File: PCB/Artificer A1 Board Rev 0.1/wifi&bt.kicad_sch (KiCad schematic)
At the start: 14 parts

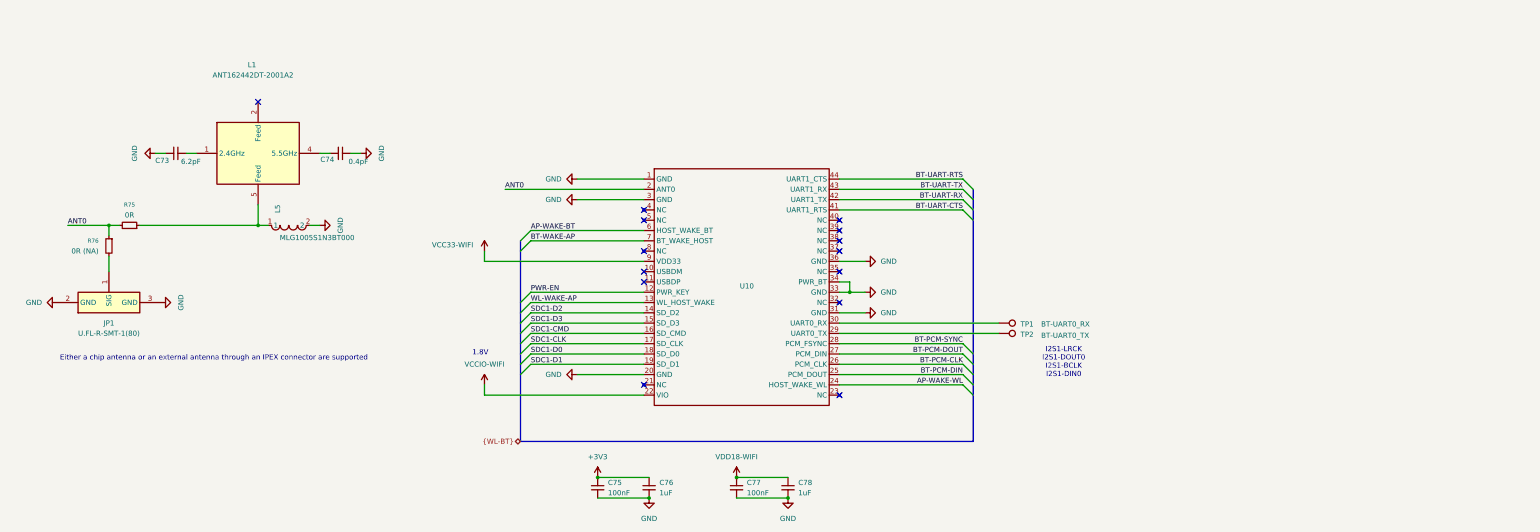
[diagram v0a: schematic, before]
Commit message: cleaned up, kicad 10 & usb c pd
migrated to Kicad 10,
added USB PD for power input
added capacitors inductors and resistor footprints
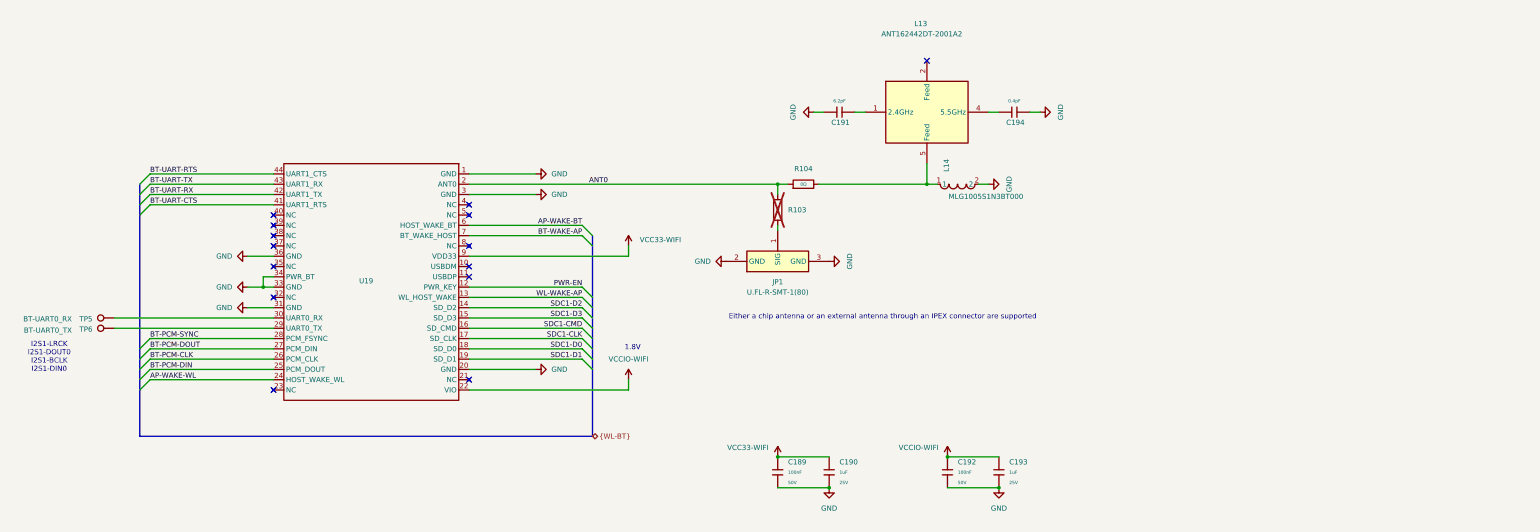
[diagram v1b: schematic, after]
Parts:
- removed C73: 6.2pF, symbol Device:C_Small
- removed C74: 0.4pF, symbol Device:C_Small
- removed C75, C77: 100nF, symbol Device:C_Small
- removed C76, C78: 1uF, symbol Device:C_Small
- removed R75: 0R, symbol Device:R_Small
- removed R76: 0R (NA), symbol Device:R_Small
- added C189, C192: 100nF, PCM_JLCPCB:C_0402, symbol PCM_JLCPCB-Capacitors:0402,100nF,(2)
- added C190, C193: 1uF, PCM_JLCPCB:C_0402, symbol PCM_JLCPCB-Capacitors:0402,1uF
- added C191: 6.2pF, PCM_JLCPCB:C_0402, symbol PCM_JLCPCB-Capacitors:0402,1pF
- added C194: 0.4pF, PCM_JLCPCB:C_0402, symbol PCM_JLCPCB-Capacitors:0402,1pF
- added R103, R104: 0Ω, PCM_JLCPCB:R_0402, symbol PCM_JLCPCB-Resistors:0402,0Ω
- U19: renamed from U10; value ~ -> (none)
- renumbered L1 to L13, L5 to L14, TP1 to TP5, TP2 to TP6
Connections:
- net ANT0: now also R103.2, R104.1
- net GND: now also C189.2, C190.2, C191.2, C192.2, C193.2, C194.1
- net VCC33-WIFI: now also C189.1, C190.1
- net VCCIO-WIFI: now also C192.1, C193.1
- net at JP1.1 (SIG): now also R103.1
- net at L13.1 (2.4GHz): now also C191.1
- net at L13.4 (5.5GHz): now also C194.2
- net at L13.5 (Feed), L14.1: now also R104.2
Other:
- moved on the sheet: JP1, L13, L14, TP5, TP6, U19

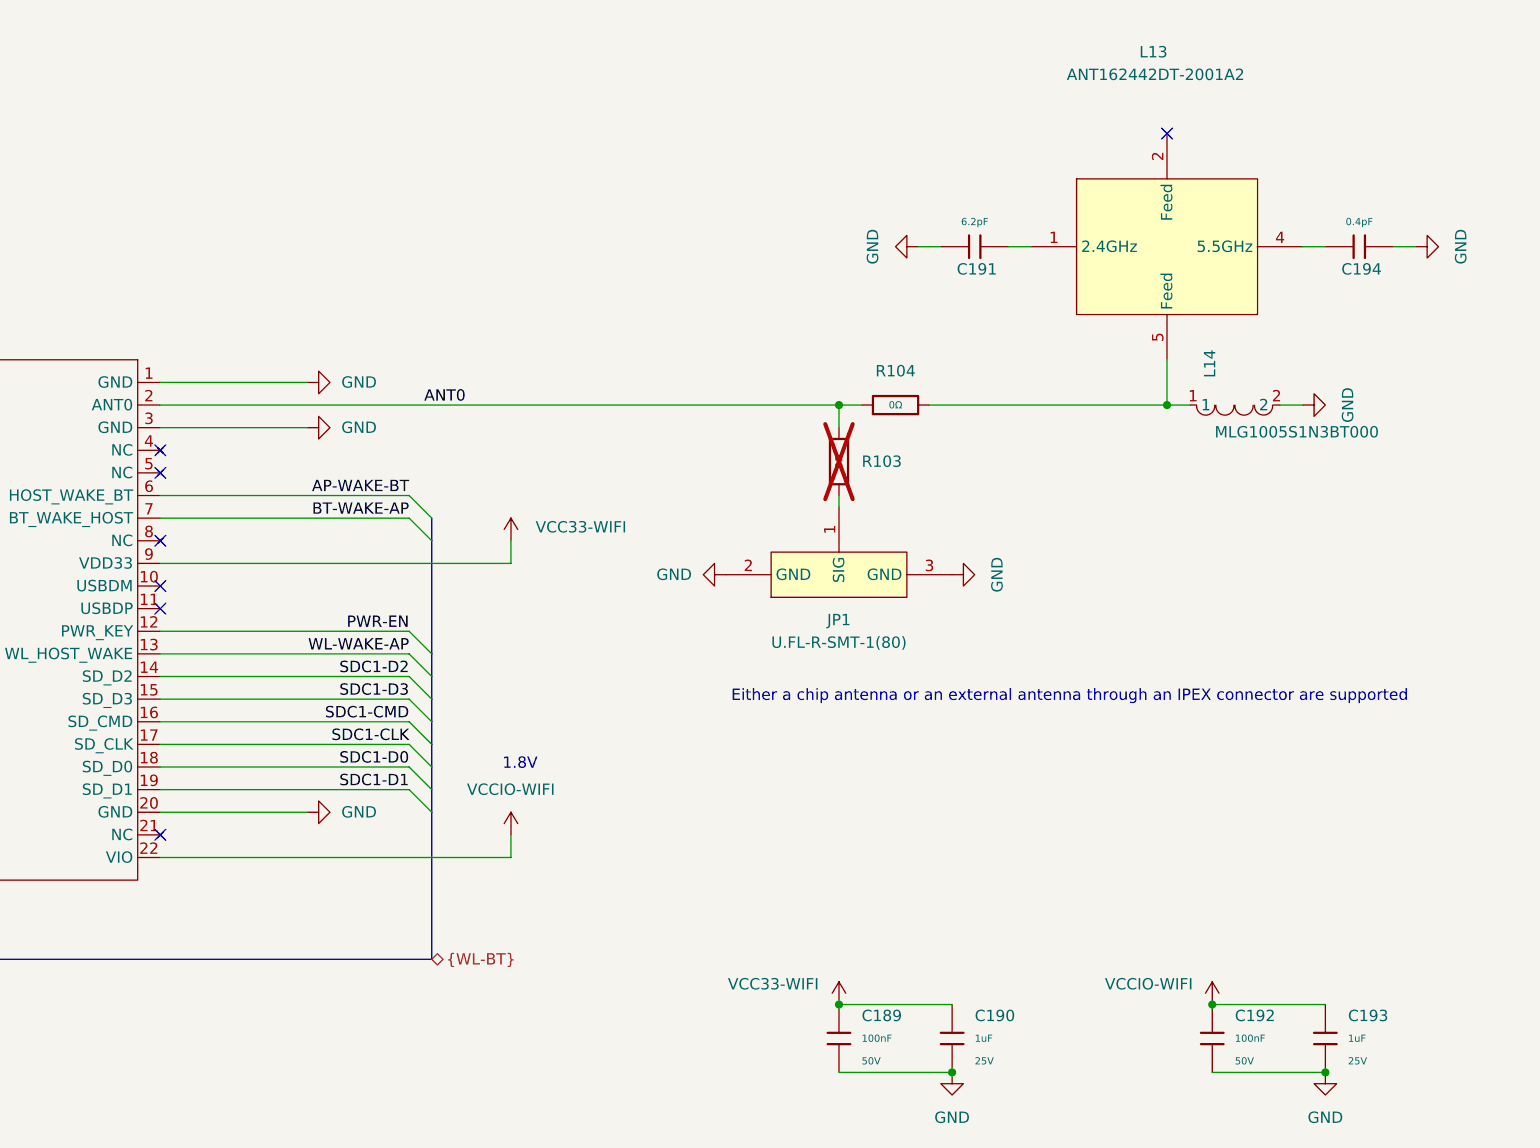
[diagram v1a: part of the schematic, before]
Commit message: placed all components
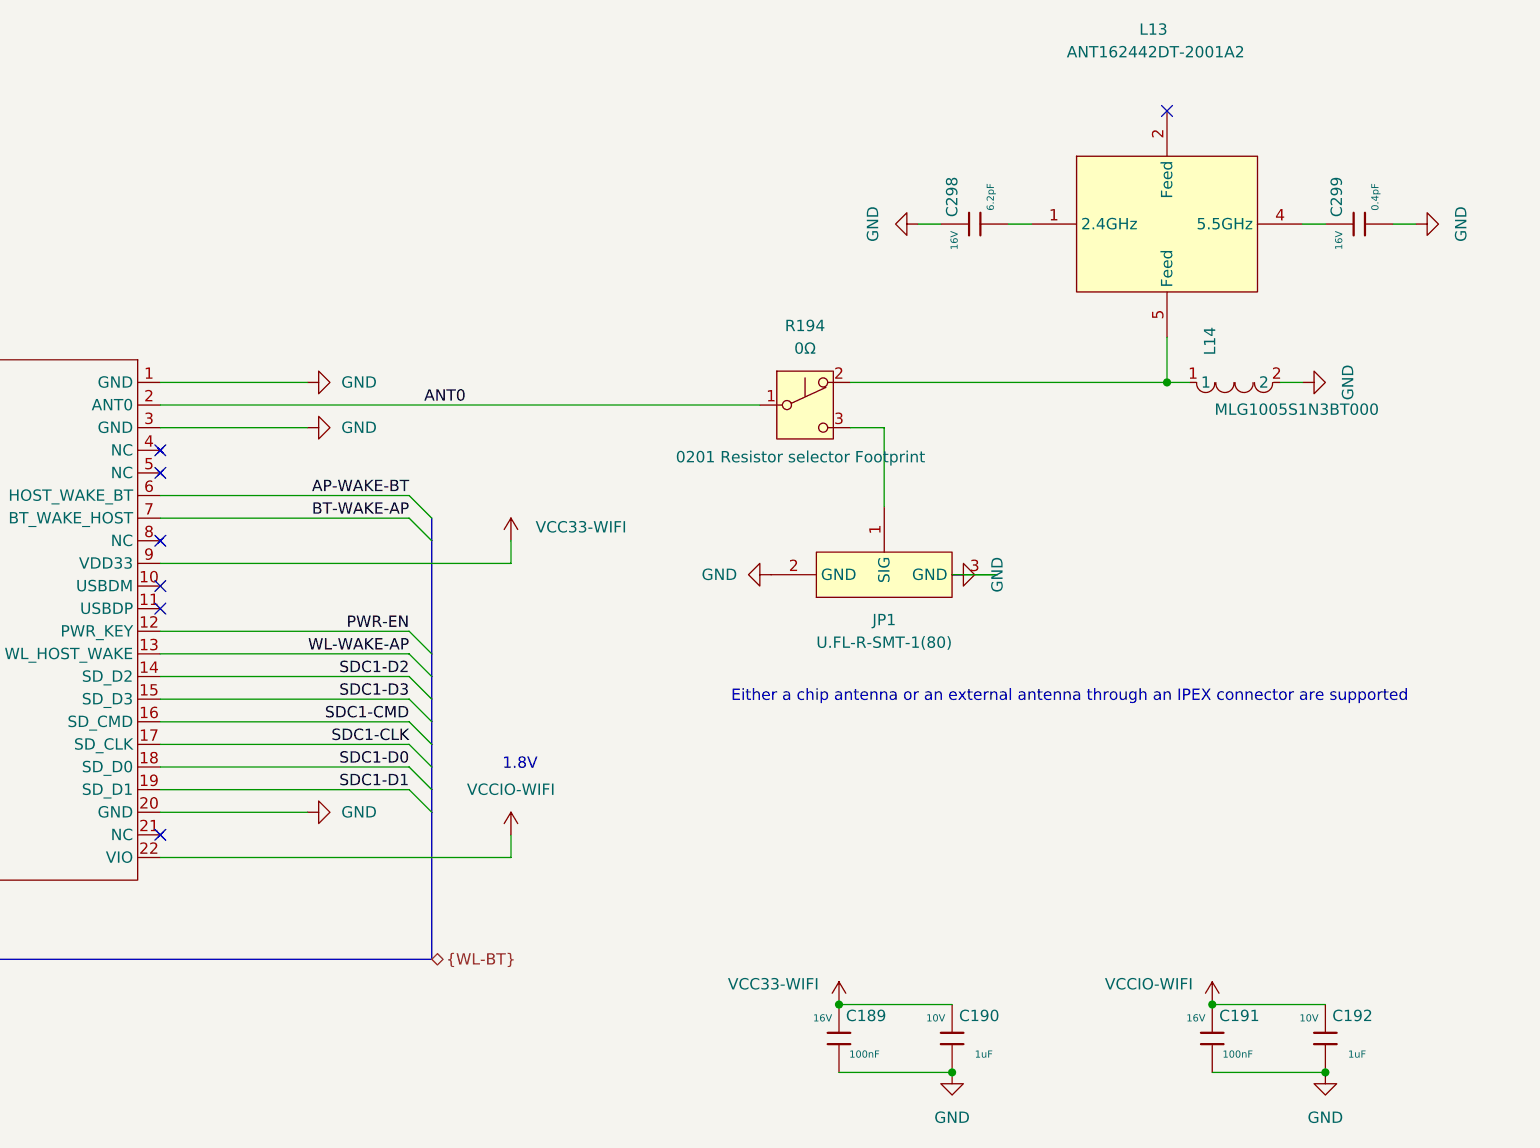
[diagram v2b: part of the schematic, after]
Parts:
- removed C189, C192: 100nF, PCM_JLCPCB:C_0402, symbol PCM_JLCPCB-Capacitors:0402,100nF,(2)
- removed C190, C193: 1uF, PCM_JLCPCB:C_0402, symbol PCM_JLCPCB-Capacitors:0402,1uF
- removed C191: 6.2pF, PCM_JLCPCB:C_0402, symbol PCM_JLCPCB-Capacitors:0402,1pF
- removed C194: 0.4pF, PCM_JLCPCB:C_0402, symbol PCM_JLCPCB-Capacitors:0402,1pF
- removed R103, R104: 0Ω, PCM_JLCPCB:R_0402, symbol PCM_JLCPCB-Resistors:0402,0Ω
- added C189, C191: 100nF, Capacitor_SMD:C_0201_0603Metric, symbol Cap:JLCPCB_Lib_Blank_Cap
- added C190, C192: 1uF, Capacitor_SMD:C_0201_0603Metric, symbol Cap:JLCPCB_Lib_Blank_Cap
- added C298: 6.2pF, Capacitor_SMD:C_0201_0603Metric, symbol Cap:JLCPCB_Lib_Blank_Cap
- added C299: 0.4pF, Capacitor_SMD:C_0201_0603Metric, symbol Cap:JLCPCB_Lib_Blank_Cap
- added R194: 0Ω, custom footprints:RF_Select_0201_L_Shape, symbol Switch:SW_Push_SPDT
- TP5, TP6: footprint (none) -> TestPoint:TestPoint_Pad_D1.0mm
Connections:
- net ANT0: now also R194.1 (B)
- net GND: now also C189.1, C190.1, C191.1, C192.1, C298.2, C299.1
- net VCC33-WIFI: now also C189.2, C190.2
- net VCCIO-WIFI: now also C191.2, C192.2
- net at JP1.1 (SIG): now also R194.3 (C)
- net at L13.1 (2.4GHz): now also C298.1
- net at L13.4 (5.5GHz): now also C299.2
- net at L13.5 (Feed), L14.1: now also R194.2 (A)
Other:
- moved on the sheet: JP1, L13, L14
